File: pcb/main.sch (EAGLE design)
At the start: 17 parts, among them J3 455-1750-1-ND, Q1 2.5A/30V/105mΩ

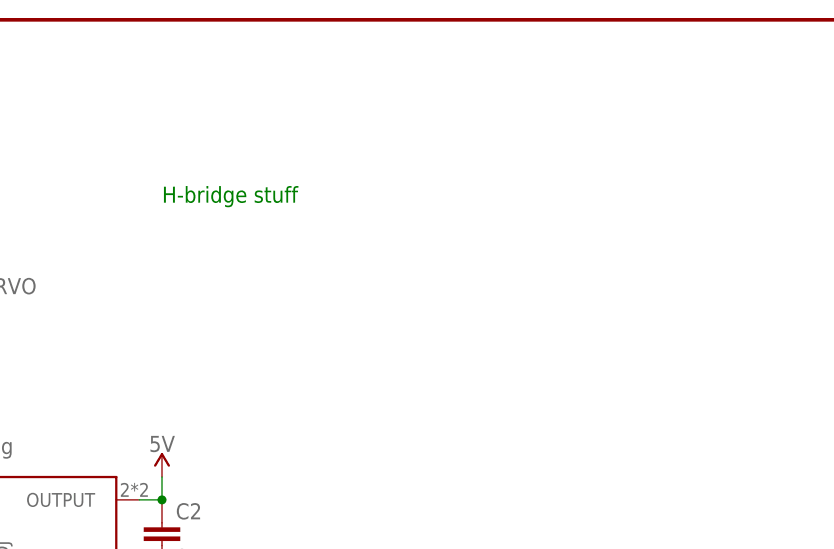
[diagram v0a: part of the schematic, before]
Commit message: added H-bridge
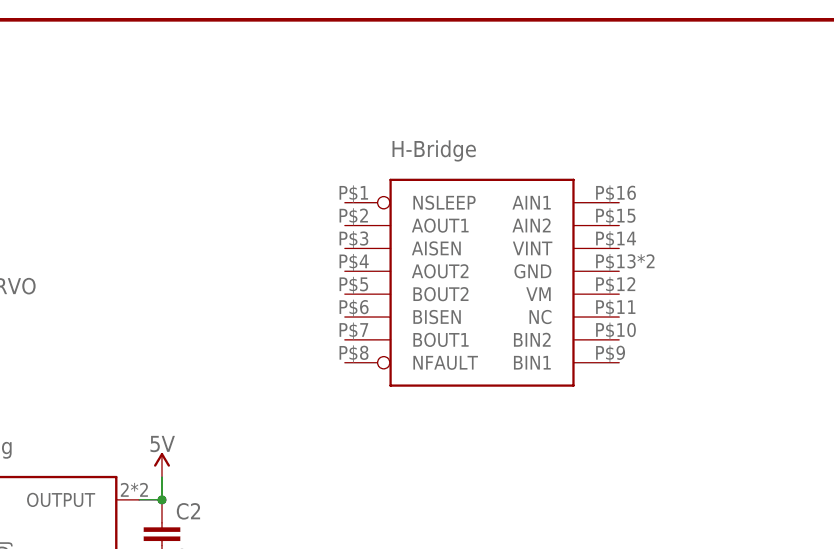
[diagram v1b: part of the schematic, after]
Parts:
- added U$2: DRV8833C, electricSheepParty:DRV8833C
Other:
- note removed: "H-bridge stuff"
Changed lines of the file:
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@@
 <attribute name="COMM" value="5-6V Lin Reg"/>
+</part>
+<part name="U$2" library="electricSheepParty" deviceset="DRV8833C" device="">
+<attribute name="COMM" value="H-Bridge"/>
 </part>
 </parts>
@@
 <sheet>
 <plain>
-<text x="1145.54" y="127" size="1.778" layer="91">H-bridge stuff</text>
 <text x="1153.16" y="63.5" size="1.778" layer="91">esp32 stuff</text>
 </plain>
@@
 <attribute name="COMM" x="1115.06" y="99.06" size="1.778" layer="96"/>
 </instance>
+<instance part="U$2" gate="G$1" x="1181.1" y="116.84">
+<attribute name="COMM" x="1170.94" y="132.08" size="1.778" layer="96"/>
+</instance>
 </instances>

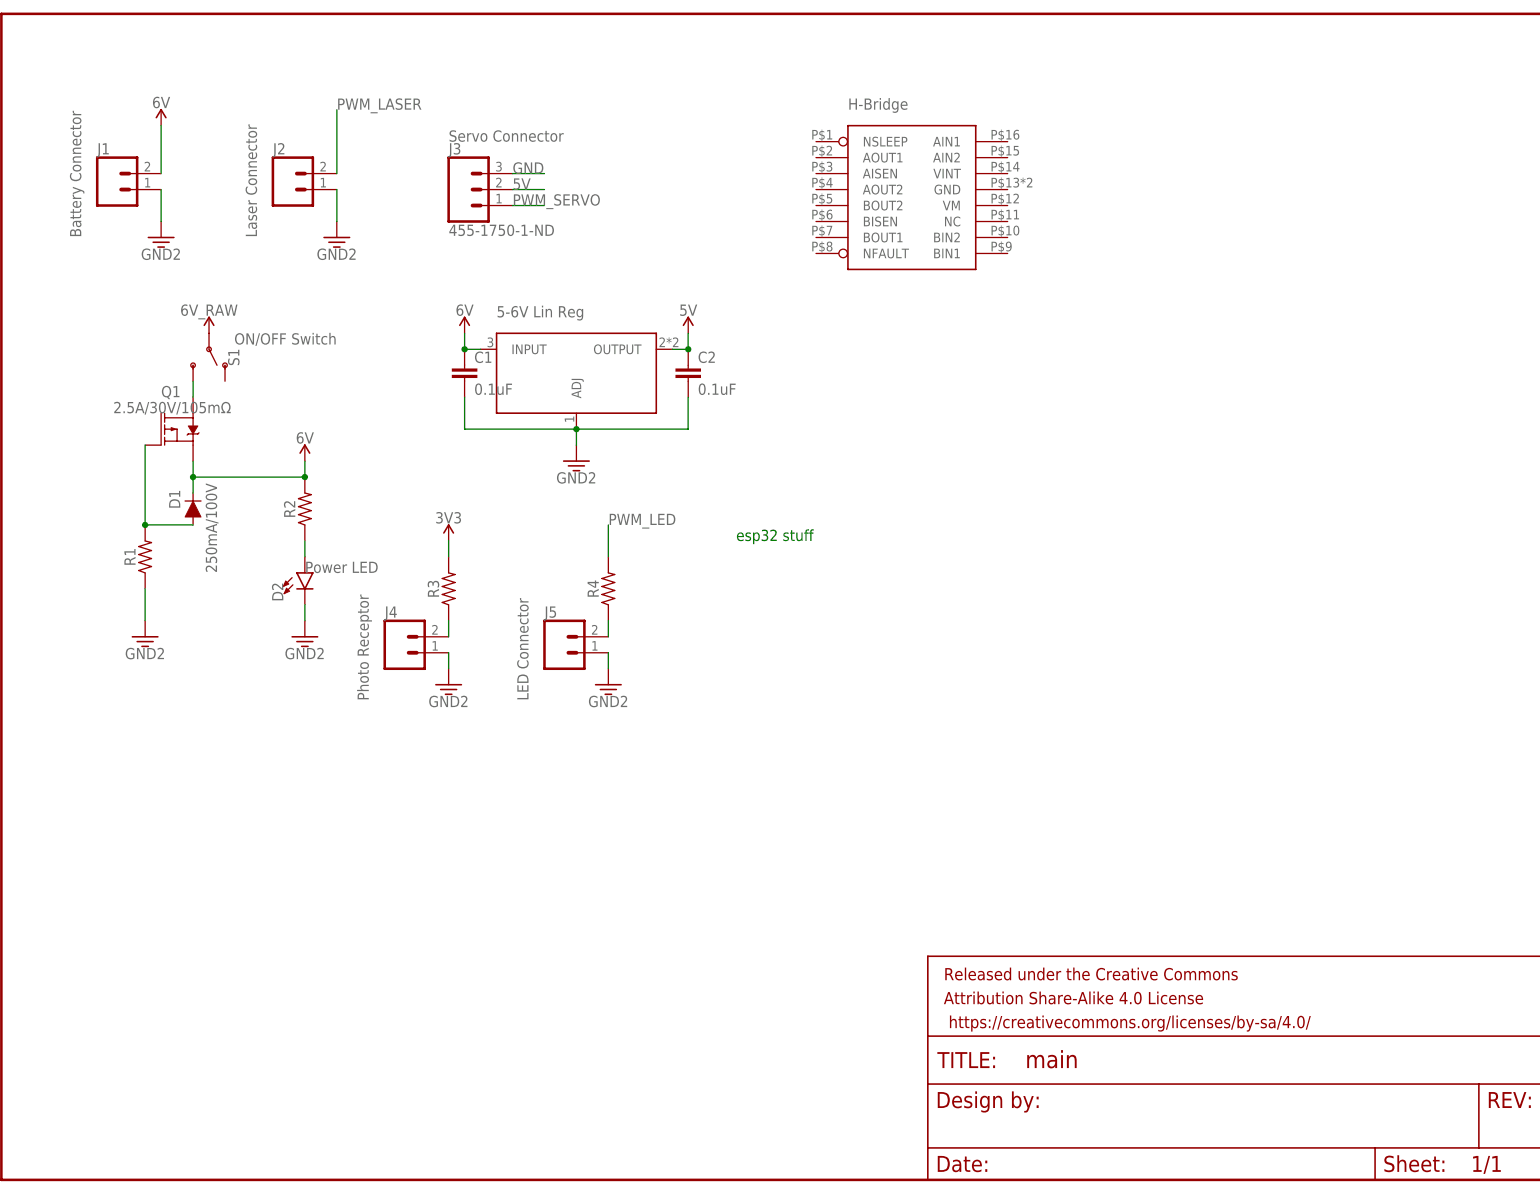
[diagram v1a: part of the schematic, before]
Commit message: added more parts, found some parts, updated BOM with more info, reorganized schematic
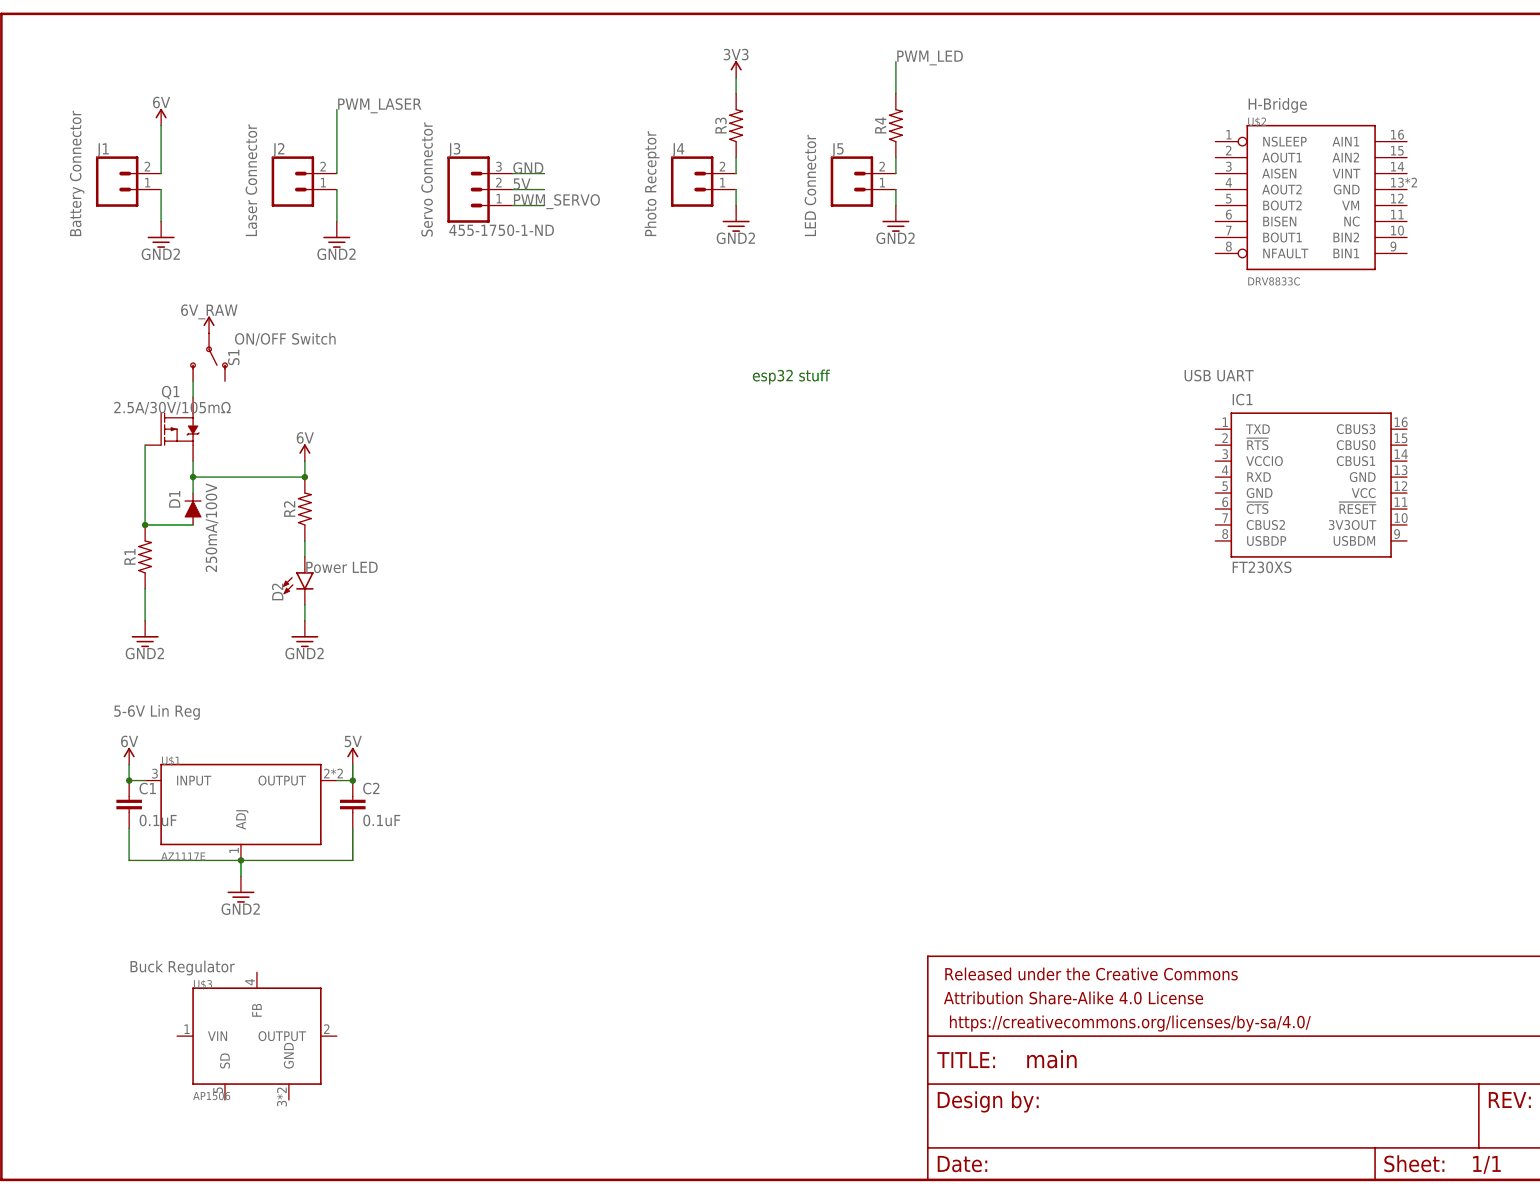
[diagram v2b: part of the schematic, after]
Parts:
- added IC1: FT230XS, electricSheepParty:FT230XS
- added U$3: AP1506, electricSheepParty:AP1506
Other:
- moved on the sheet: C1, C2, J4, J5, R3, R4
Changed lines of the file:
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@@
 <attribute name="COMM" value="H-Bridge"/>
+</part>
+<part name="U$3" library="electricSheepParty" deviceset="AP1506" device="">
+<attribute name="COMM" value="Buck Regulator"/>
+</part>
+<part name="IC1" library="electricSheepParty" deviceset="FT230X" device="S">
+<attribute name="COMM" value="USB UART"/>
 </part>
 </parts>
@@
 <sheet>
 <plain>
-<text x="1153.16" y="63.5" size="1.778" layer="91">esp32 stuff</text>
+<text x="1155.7" y="88.9" size="1.778" layer="91">esp32 stuff</text>
 </plain>
 <instances>
@@
 <instance part="GND2" gate="G$1" x="1089.66" y="111.76"/>
 <instance part="J3" gate="J$1" x="1109.98" y="119.38">
-<attribute name="COMM" x="1107.44" y="127" size="1.778" layer="96"/>
+<attribute name="COMM" x="1104.9" y="111.76" size="1.778" layer="96" rot="R90"/>
 </instance>
 <instance part="R1" gate="G$1" x="1059.18" y="60.96" rot="R90"/>
@@
 <attribute name="COMMENT" x="1084.58" y="58.42" size="1.778" layer="96"/>
 </instance>
-<instance part="J4" gate="G$1" x="1099.82" y="45.72" smashed="yes">
-<attribute name="COMM" x="1094.74" y="38.1" size="1.778" layer="96" rot="R90"/>
-<attribute name="VALUE" x="1097.28" y="40.894" size="1.778" layer="96" font="vector"/>
-<attribute name="NAME" x="1097.28" y="51.308" size="1.778" layer="95" font="vector"/>
-</instance>
-<instance part="J5" gate="G$1" x="1125.22" y="45.72">
-<attribute name="COMM" x="1120.14" y="38.1" size="1.778" layer="96" rot="R90"/>
-</instance>
-<instance part="SUPPLY4" gate="G$1" x="1107.44" y="63.5"/>
-<instance part="R3" gate="G$1" x="1107.44" y="55.88" rot="R90"/>
-<instance part="R4" gate="G$1" x="1132.84" y="55.88" rot="R90"/>
-<instance part="GND5" gate="G$1" x="1107.44" y="40.64"/>
-<instance part="GND6" gate="G$1" x="1132.84" y="40.64"/>
-<instance part="C1" gate="G$1" x="1109.98" y="88.9"/>
-<instance part="C2" gate="G$1" x="1145.54" y="88.9"/>
-<instance part="SUPPLY5" gate="G$1" x="1109.98" y="96.52"/>
-<instance part="SUPPLY6" gate="G$1" x="1145.54" y="96.52"/>
-<instance part="GND7" gate="G$1" x="1127.76" y="76.2"/>
-<instance part="U$1" gate="G$1" x="1115.06" y="83.82">
-<attribute name="COMM" x="1115.06" y="99.06" size="1.778" layer="96"/>
-</instance>
-<instance part="U$2" gate="G$1" x="1181.1" y="116.84">
-<attribute name="COMM" x="1170.94" y="132.08" size="1.778" layer="96"/>
+<instance part="J4" gate="G$1" x="1145.54" y="119.38" smashed="yes">
+<attribute name="COMM" x="1140.46" y="111.76" size="1.778" layer="96" rot="R90"/>
+<attribute name="VALUE" x="1143" y="114.554" size="1.778" layer="96" font="vector"/>
+<attribute name="NAME" x="1143" y="124.968" size="1.778" layer="95" font="vector"/>
+</instance>
+<instance part="J5" gate="G$1" x="1170.94" y="119.38">
+<attribute name="COMM" x="1165.86" y="111.76" size="1.778" layer="96" rot="R90"/>
+</instance>
+<instance part="SUPPLY4" gate="G$1" x="1153.16" y="137.16"/>
+<instance part="R3" gate="G$1" x="1153.16" y="129.54" rot="R90"/>
+<instance part="R4" gate="G$1" x="1178.56" y="129.54" rot="R90"/>
+<instance part="GND5" gate="G$1" x="1153.16" y="114.3"/>
+<instance part="GND6" gate="G$1" x="1178.56" y="114.3"/>
+<instance part="C1" gate="G$1" x="1056.64" y="20.32"/>
+<instance part="C2" gate="G$1" x="1092.2" y="20.32"/>
+<instance part="SUPPLY5" gate="G$1" x="1056.64" y="27.94"/>
+<instance part="SUPPLY6" gate="G$1" x="1092.2" y="27.94"/>
+<instance part="GND7" gate="G$1" x="1074.42" y="7.62"/>
+<instance part="U$1" gate="G$1" x="1074.42" y="20.32">
+<attribute name="COMM" x="1054.1" y="35.56" size="1.778" layer="96"/>
+</instance>
+<instance part="U$2" gate="G$1" x="1244.6" y="116.84">
+<attribute name="COMM" x="1234.44" y="132.08" size="1.778" layer="96"/>
+</instance>
+<instance part="U$3" gate="G$1" x="1076.96" y="-15.24">
+<attribute name="COMM" x="1056.64" y="-5.08" size="1.778" layer="96"/>
+</instance>
+<instance part="IC1" gate="G$1" x="1244.6" y="73.66">
+<attribute name="COMM" x="1224.28" y="88.9" size="1.778" layer="96"/>
 </instance>
 </instances>
@@
 <pinref part="SUPPLY4" gate="G$1" pin="VCC"/>
 <pinref part="R3" gate="G$1" pin="2"/>
-<wire x1="1107.44" y1="63.5" x2="1107.44" y2="60.96" width="0.1524" layer="91"/>
+<wire x1="1153.16" y1="137.16" x2="1153.16" y2="134.62" width="0.1524" layer="91"/>
 </segment>
 <segment>
 <pinref part="SUPPLY5" gate="G$1" pin="VCC"/>
 <pinref part="C1" gate="G$1" pin="1"/>
-<wire x1="1109.98" y1="96.52" x2="1109.98" y2="93.98" width="0.1524" layer="91"/>
-<wire x1="1109.98" y1="93.98" x2="1112.52" y2="93.98" width="0.1524" layer="91"/>
-<junction x="1109.98" y="93.98"/>
+<wire x1="1056.64" y1="27.94" x2="1056.64" y2="25.4" width="0.1524" layer="91"/>
+<wire x1="1056.64" y1="25.4" x2="1059.18" y2="25.4" width="0.1524" layer="91"/>
+<junction x="1056.64" y="25.4"/>
 <pinref part="U$1" gate="G$1" pin="INPUT"/>
 </segment>
@@
 <pinref part="SUPPLY6" gate="G$1" pin="VCC"/>
 <pinref part="C2" gate="G$1" pin="1"/>
-<wire x1="1145.54" y1="96.52" x2="1145.54" y2="93.98" width="0.1524" layer="91"/>
-<wire x1="1145.54" y1="93.98" x2="1143" y2="93.98" width="0.1524" layer="91"/>
-<junction x="1145.54" y="93.98"/>
+<wire x1="1092.2" y1="27.94" x2="1092.2" y2="25.4" width="0.1524" layer="91"/>
+<wire x1="1092.2" y1="25.4" x2="1089.66" y2="25.4" width="0.1524" layer="91"/>
+<junction x="1092.2" y="25.4"/>
 <pinref part="U$1" gate="G$1" pin="OUTPUT"/>
 </segment>
@@
 <pinref part="J4" gate="G$1" pin="1"/>
 <pinref part="GND5" gate="G$1" pin="3.3V"/>
-<wire x1="1107.44" y1="45.72" x2="1107.44" y2="43.18" width="0.1524" layer="91"/>
+<wire x1="1153.16" y1="119.38" x2="1153.16" y2="116.84" width="0.1524" layer="91"/>
 </segment>
 <segment>
 <pinref part="GND6" gate="G$1" pin="3.3V"/>
 <pinref part="J5" gate="G$1" pin="1"/>
-<wire x1="1132.84" y1="43.18" x2="1132.84" y2="45.72" width="0.1524" layer="91"/>
+<wire x1="1178.56" y1="116.84" x2="1178.56" y2="119.38" width="0.1524" layer="91"/>
 </segment>
 <segment>
 <pinref part="C1" gate="G$1" pin="2"/>
 <pinref part="U$1" gate="G$1" pin="ADJ"/>
-<wire x1="1109.98" y1="86.36" x2="1109.98" y2="81.28" width="0.1524" layer="91"/>
-<wire x1="1109.98" y1="81.28" x2="1127.76" y2="81.28" width="0.1524" layer="91"/>
+<wire x1="1056.64" y1="17.78" x2="1056.64" y2="12.7" width="0.1524" layer="91"/>
+<wire x1="1056.64" y1="12.7" x2="1074.42" y2="12.7" width="0.1524" layer="91"/>
 <pinref part="C2" gate="G$1" pin="2"/>
-<wire x1="1145.54" y1="86.36" x2="1145.54" y2="81.28" width="0.1524" layer="91"/>
-<wire x1="1145.54" y1="81.28" x2="1127.76" y2="81.28" width="0.1524" layer="91"/>
-<junction x="1127.76" y="81.28"/>
+<wire x1="1092.2" y1="17.78" x2="1092.2" y2="12.7" width="0.1524" layer="91"/>
+<wire x1="1092.2" y1="12.7" x2="1074.42" y2="12.7" width="0.1524" layer="91"/>
+<junction x="1074.42" y="12.7"/>
 <pinref part="GND7" gate="G$1" pin="3.3V"/>
-<wire x1="1127.76" y1="81.28" x2="1127.76" y2="78.74" width="0.1524" layer="91"/>
+<wire x1="1074.42" y1="12.7" x2="1074.42" y2="10.16" width="0.1524" layer="91"/>
 </segment>
 </net>
@@
 <pinref part="J4" gate="G$1" pin="2"/>
 <pinref part="R3" gate="G$1" pin="1"/>
-<wire x1="1107.44" y1="48.26" x2="1107.44" y2="50.8" width="0.1524" layer="91"/>
+<wire x1="1153.16" y1="121.92" x2="1153.16" y2="124.46" width="0.1524" layer="91"/>
 </segment>
 </net>
@@
 <pinref part="J5" gate="G$1" pin="2"/>
 <pinref part="R4" gate="G$1" pin="1"/>
-<wire x1="1132.84" y1="48.26" x2="1132.84" y2="50.8" width="0.1524" layer="91"/>
+<wire x1="1178.56" y1="121.92" x2="1178.56" y2="124.46" width="0.1524" layer="91"/>
 </segment>
 </net>
@@
 <segment>
 <pinref part="R4" gate="G$1" pin="2"/>
-<wire x1="1132.84" y1="60.96" x2="1132.84" y2="66.04" width="0.1524" layer="91"/>
-<label x="1132.84" y="66.04" size="1.778" layer="95"/>
-</segment>
-</net>
+<wire x1="1178.56" y1="134.62" x2="1178.56" y2="139.7" width="0.1524" layer="91"/>
+<label x="1178.56" y="139.7" size="1.778" layer="95"/>
+</segment>
+</net>
